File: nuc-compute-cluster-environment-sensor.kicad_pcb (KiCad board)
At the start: 4 copper layers, 50 x 26.5 mm, 123 parts, among them J1 USB4105-GF-A, J2 SM04B-SRSS-TB-LF-SN, J3 SM04B-SRSS-TB-LF-SN, U1 FT4232H-56Q, U2 AP7370-33SA-7, U3 STM32G474CET6, U4 MB85RC1MTPNF-G, U5 SHT45, U6 BME280, Y1 ABM3B-12.000MHZ-B2-T, Y2 ECS-_327-12_5-34B-TR, Y3 ABM3B-8.000MHZ-10-1-U-T

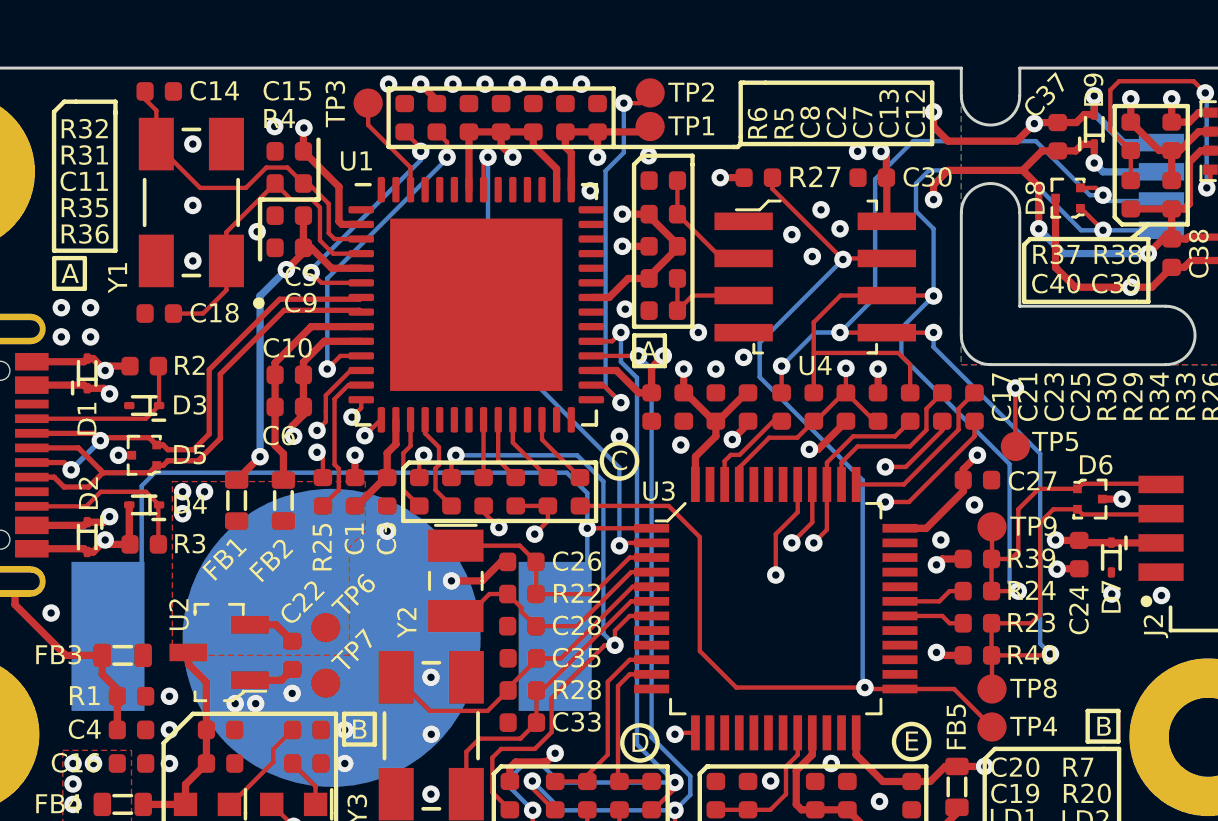
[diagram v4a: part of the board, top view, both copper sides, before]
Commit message: Final tweaks, removing vias from the logos
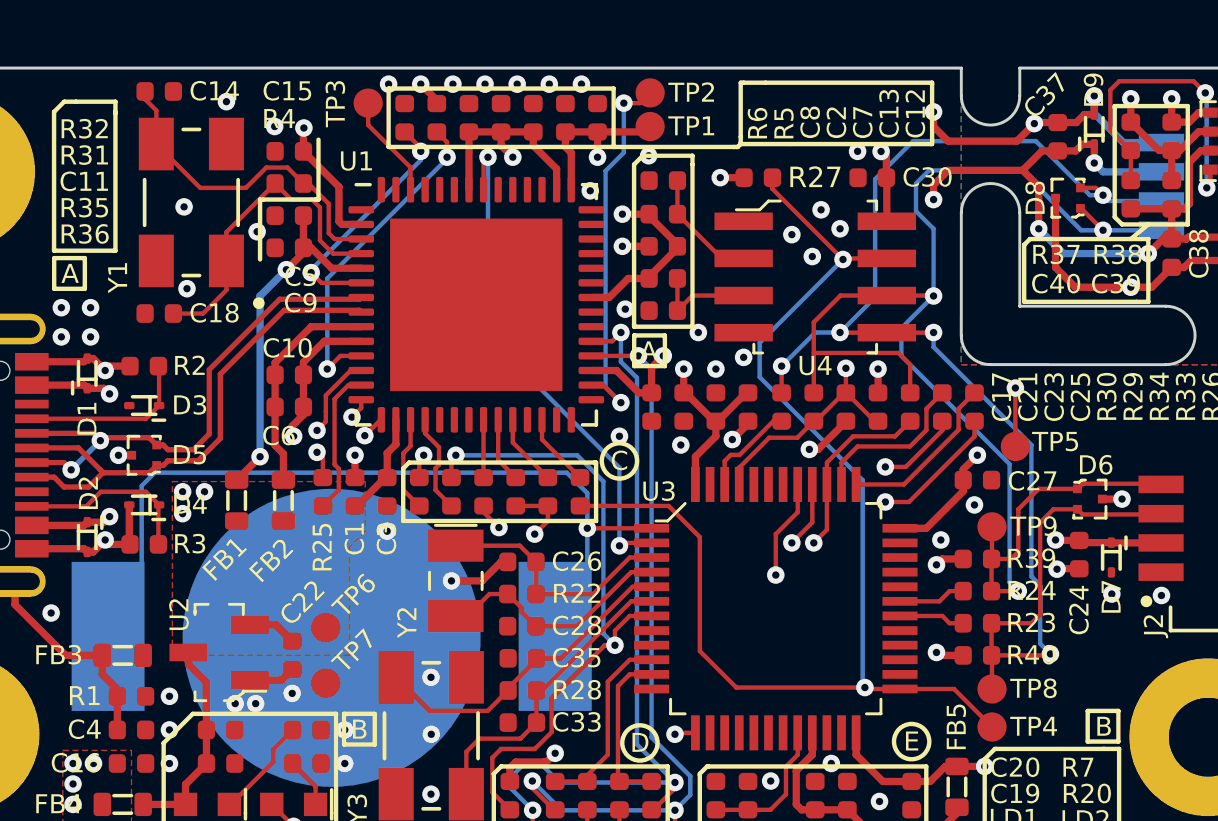
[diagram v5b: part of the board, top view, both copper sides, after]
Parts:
- moved REF** 0.36 mm to (204.8, 128.5)
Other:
- board text added: "Rev. 1.0.1 01/2023"
- board text removed: "Rev. 1.0.1 01/2022"
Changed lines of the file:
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@@
   )
   (footprint "antmicro-footprints:OSHW-Logo_7.5x8mm_Mask" (layer "B.Cu")
-    (at 205.2 128.4 -90)
+    (at 204.85 128.5 -90)
     (descr "Open Source Hardware Logo")
     (tags "Logo OSHW")
@@
   )
   (gr_text "Environment Sensor" (at 172 121.7 90) (layer "B.Mask")
-    (effects (font (size 0.65 0.65) (thickness 0.15) italic) (justify mirror))
+    (effects (font (size 0.65 0.65) (thickness 0.15)) (justify mirror))
   )
-  (gr_text "Rev. 1.0.1 01/2022" (at 173 121.7 90) (layer "B.Mask")
-    (effects (font (size 0.65 0.65) (thickness 0.15) italic) (justify mirror))
+  (gr_text "Rev. 1.0.1 01/2023" (at 172.95 121.8 90) (layer "B.Mask")
+    (effects (font (size 0.65 0.65) (thickness 0.15)) (justify mirror))
   )
   (segment (start 168.24 123.44) (end 168.65 123.85) (width 0.25) (layer "F.Cu") (net 1))
@@
   (via (at 197.25 129.65) (size 0.6) (drill 0.25) (layers "F.Cu" "B.Cu") (net 1))
   (via (at 203.75 121) (size 0.6) (drill 0.25) (layers "F.Cu" "B.Cu") (net 1))
-  (via (at 171.65 118.2) (size 0.6) (drill 0.25) (layers "F.Cu" "B.Cu") (net 1))
+  (via (at 171.35 118.25) (size 0.6) (drill 0.25) (layers "F.Cu" "B.Cu") (net 1))
   (via (at 183.85 114.05) (size 0.6) (drill 0.25) (layers "F.Cu" "B.Cu") (net 1))
-  (via (at 171.65 120.1) (size 0.6) (drill 0.25) (layers "F.Cu" "B.Cu") (net 1))
+  (via (at 171.45 121.05) (size 0.6) (drill 0.25) (layers "F.Cu" "B.Cu") (net 1))
   (via (at 176.85 136.15) (size 0.6) (drill 0.25) (layers "F.Cu" "B.Cu") (net 1))
   (via (at 185.2505 117.7) (size 0.6) (drill 0.25) (layers "F.Cu" "B.Cu") (net 1))
@@
   (via (at 186.25 126.1) (size 0.6) (drill 0.25) (layers "F.Cu" "B.Cu") (net 1))
   (via (at 168.65 129.65) (size 0.6) (drill 0.25) (layers "F.Cu" "B.Cu") (net 1))
-  (via (at 171.65 116.1) (size 0.6) (drill 0.25) (layers "F.Cu" "B.Cu") (net 1))
+  (via (at 172.8 114.65) (size 0.6) (drill 0.25) (layers "F.Cu" "B.Cu") (net 1))
   (via (at 170.85 136.15) (size 0.6) (drill 0.25) (layers "F.Cu" "B.Cu") (net 1))
   (via (at 188.35 126.4) (size 0.6) (drill 0.25) (layers "F.Cu" "B.Cu") (net 1))
@@
   (segment (start 183.35 129.45) (end 186.8 132.9) (width 0.15) (layer "In2.Cu") (net 23))
   (segment (start 195 121.35) (end 195 117.3) (width 0.15) (layer "B.Cu") (net 23))
+  (segment (start 200.35 130.9) (end 200.35 126.4) (width 0.15) (layer "B.Cu") (net 23))
+  (segment (start 200.6495 131.1995) (end 200.35 130.9) (width 0.15) (layer "B.Cu") (net 23))
+  (segment (start 200.6495 133.1995) (end 200.6495 131.1995) (width 0.15) (layer "B.Cu") (net 23))
   (segment (start 193.8 122.55) (end 192.95 122.55) (width 0.15) (layer "B.Cu") (net 23))
   (segment (start 202.35 117.85) (end 202.8 117.85) (width 0.15) (layer "B.Cu") (net 23))
+  (segment (start 200.35 126.4) (end 197 123.05) (width 0.15) (layer "B.Cu") (net 23))
+  (segment (start 197 123.05) (end 197 122.55) (width 0.15) (layer "B.Cu") (net 23))
   (segment (start 203 118.05) (end 204.8 118.05) (width 0.15) (layer "B.Cu") (net 23))
   (segment (start 201 133.55) (end 200.6495 133.1995) (width 0.15) (layer "B.Cu") (net 23))
-  (segment (start 197 123.05) (end 197 122.55) (width 0.15) (layer "B.Cu") (net 23))
-  (segment (start 200.6495 126.6995) (end 197 123.05) (width 0.15) (layer "B.Cu") (net 23))
   (segment (start 192.95 122.55) (end 191.8 123.7) (width 0.15) (layer "B.Cu") (net 23))
   (segment (start 195 117.3) (end 196.3 116) (width 0.15) (layer "B.Cu") (net 23))
@@
   (segment (start 202.8 117.85) (end 203 118.05) (width 0.15) (layer "B.Cu") (net 23))
   (segment (start 193.8 122.55) (end 195 121.35) (width 0.15) (layer "B.Cu") (net 23))
-  (segment (start 200.6495 133.1995) (end 200.6495 126.6995) (width 0.15) (layer "B.Cu") (net 23))
   (segment (start 196.3 116) (end 200.5 116) (width 0.15) (layer "B.Cu") (net 23))
   (segment (start 208.66 132.05) (end 208.66 126.45) (width 0.15) (layer "F.Cu") (net 26))

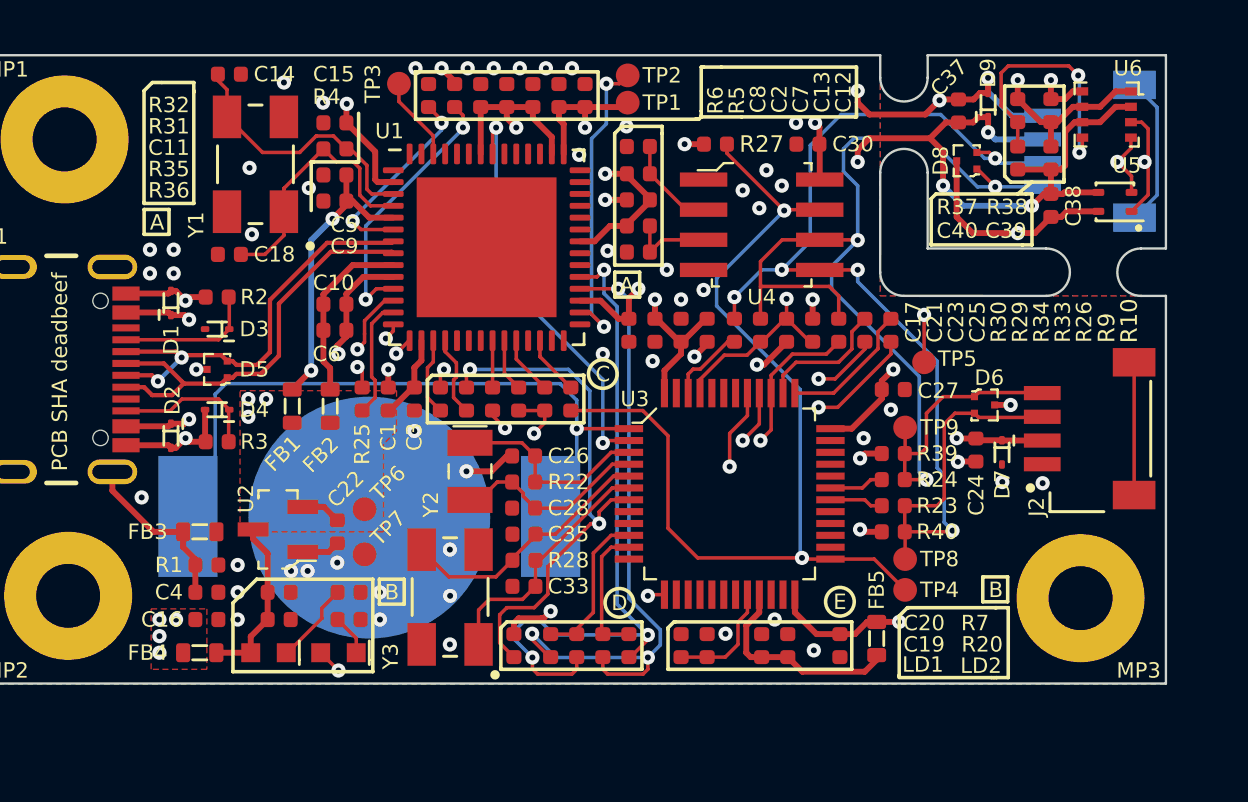
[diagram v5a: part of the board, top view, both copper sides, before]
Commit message: Small tweaks on schematic comments and PCB silkscreen, exported wrl models, README finished
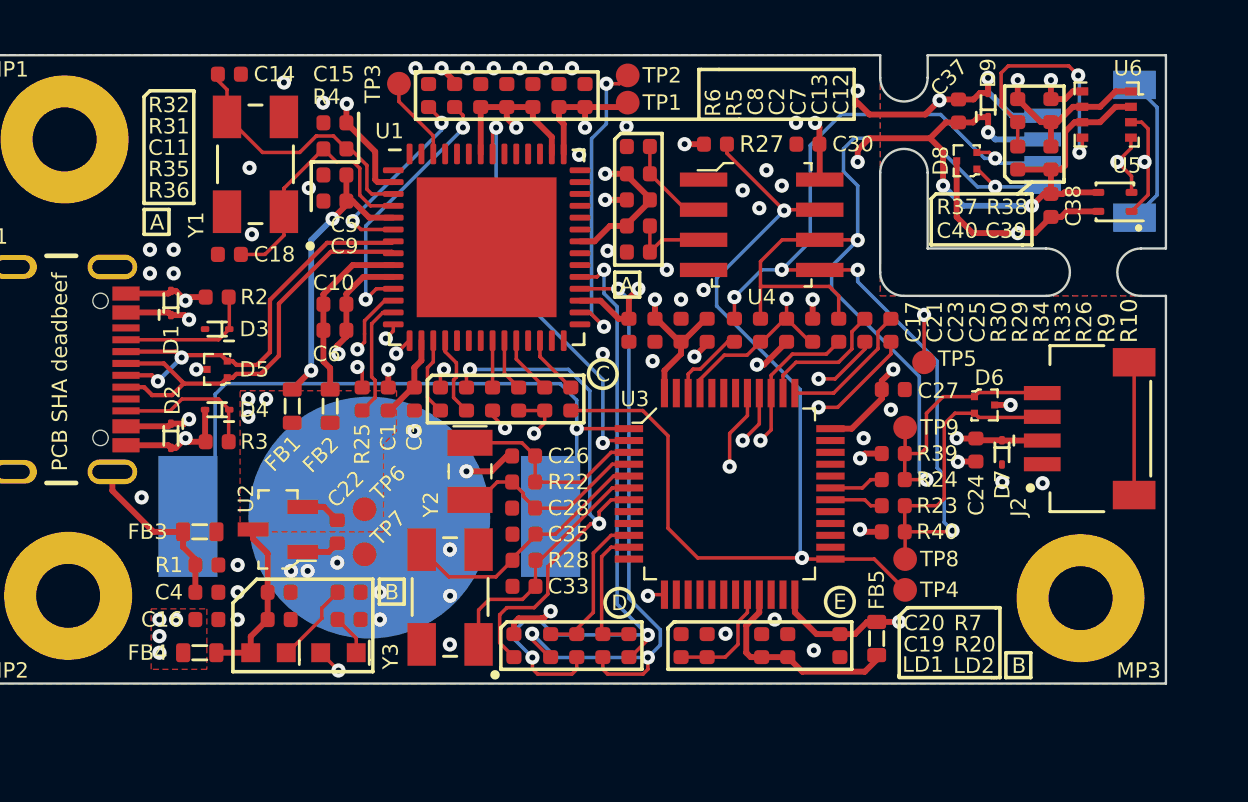
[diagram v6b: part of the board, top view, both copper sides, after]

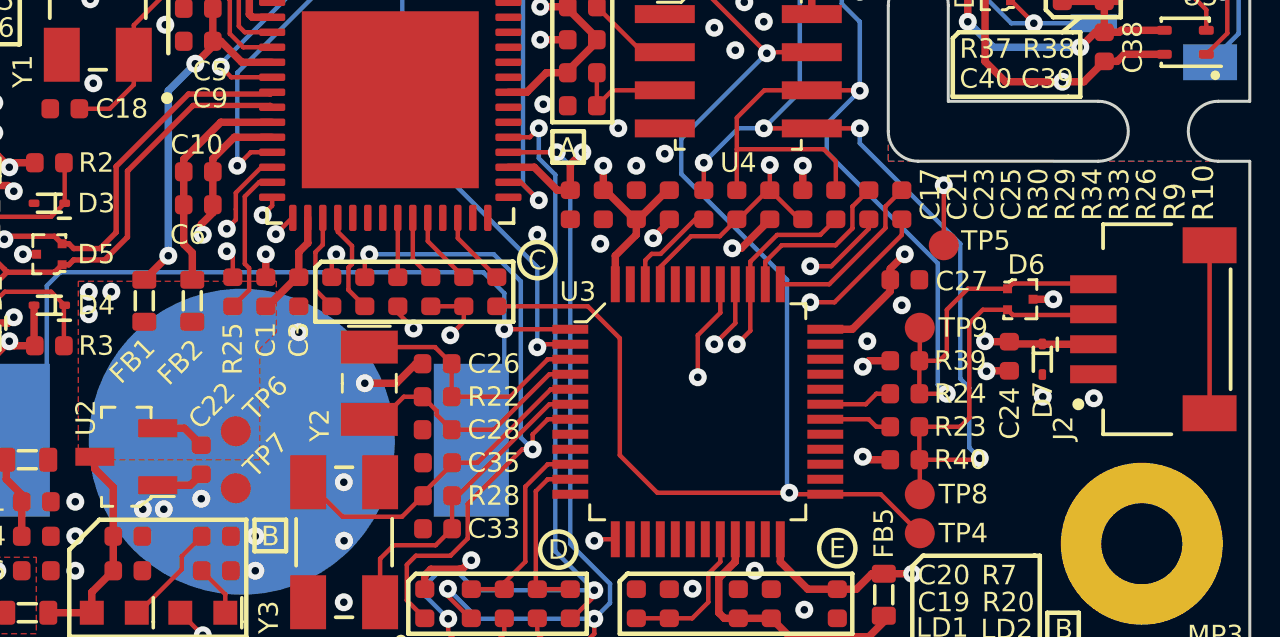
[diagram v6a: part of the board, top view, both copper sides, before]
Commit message: Fixed connection of SWD/JTAG configuration resistors
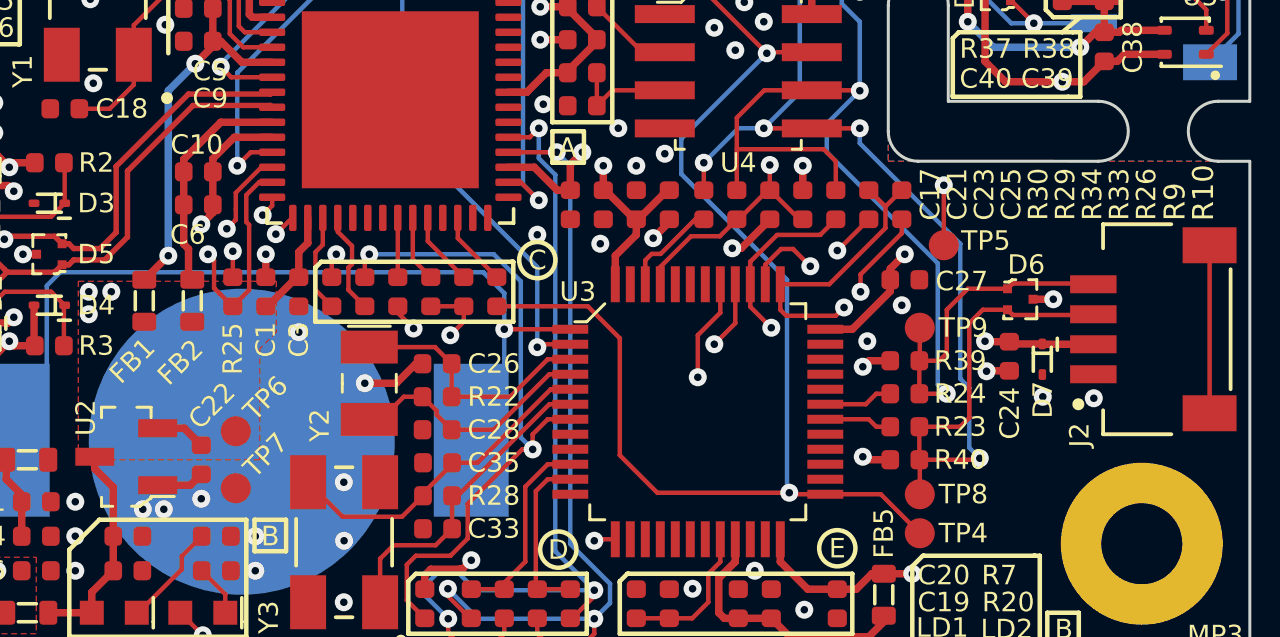
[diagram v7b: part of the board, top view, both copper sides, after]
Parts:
- removed REF**: OSHW-Logo_7.5x8mm_Mask, antmicro-footprints:OSHW-Logo_7.5x8mm_Mask
- C13, C15: value C_4u7_0402 -> C_100n_0402
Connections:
- R10 pad 2: Net-(U1-Pad15) -> JTDO
- R9 pad 1: SWCLK-JTCK -> SWDIO-JTMS
- R9 pad 2: Net-(U1-Pad12) -> JTDI
- U1 pad 12: Net-(U1-Pad12) -> SWCLK-JTCK
- U1 pad 15: Net-(U1-Pad15) -> SWDIO-JTMS
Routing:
- net JTDI: track 5.05 -> 35.5 mm, vias 0 -> 2
- net Net-(U1-Pad12): track 28.8 -> 0.00 mm, vias 2 -> 0
- net SWDIO-JTMS: track 5.77 -> 32.4 mm, vias 0 -> 2
- net Net-(U1-Pad15): track 26.1 -> 0.00 mm, vias 2 -> 0
- net SWCLK-JTCK: track 5.61 -> 28.6 mm, vias 0 -> 2
- net JTDO: track 20.2 -> 29.2 mm, vias 2 -> 3
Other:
- board text added: "Rev. 1.0.2 01/2023"
- board text removed: "Rev. 1.0.1 01/2023"
